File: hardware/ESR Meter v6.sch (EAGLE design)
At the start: 34 parts, among them Q1 MOSFET-NCHANNELFQP30N06L, U1 ATMEGA328P, U2 3V3, U3 LM317, Y1 8M

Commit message: Update library used for L4931
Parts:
- U2: device RBBB:L4931 -> l4931:L4931
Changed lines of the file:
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@@
 <part name="R2" library="resistor" deviceset="R-US_" device="0207/10" value="2.2k"/>
 <part name="SUPPLY1" library="supply2" deviceset="GND" device=""/>
-<part name="U2" library="RBBB" deviceset="L4931" device="" value="3V3"/>
+<part name="U2" library="l4931" deviceset="L4931" device="" value="3V3"/>
 <part name="C1" library="SparkFun-Capacitors" deviceset="CAP_POL" device="PTH2" value="47u"/>
 <part name="C2" library="SparkFun-Capacitors" deviceset="CAP_POL" device="PTH2" value="47u"/>

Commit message: Rewrote README.md
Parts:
- R8: value 1 -> 1 1%
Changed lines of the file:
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@@
 <part name="SUPPLY9" library="supply2" deviceset="GND" device=""/>
 <part name="Q1" library="SparkFun-DiscreteSemi" deviceset="MOSFET-NCHANNEL" device="FQP30N06L"/>
-<part name="R8" library="resistor" deviceset="R-US_" device="0617/5V" value="1"/>
+<part name="R8" library="resistor" deviceset="R-US_" device="0617/5V" value="1 1%"/>
 <part name="SUPPLY10" library="supply2" deviceset="GND" device=""/>
 <part name="D1" library="diode" deviceset="1N581*" device="" technology="9-B"/>

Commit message: Edited README
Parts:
- Q1: value MOSFET-NCHANNELFQP30N06L -> FQP30N06L
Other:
- moved on the sheet: BATT+, BATT-, C1, C2, JP3, PAD1, PAD2, U2
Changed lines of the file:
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@@
 <part name="LOGO1" library="SparkFun-Aesthetics" deviceset="OSHW-LOGO" device="M"/>
 <part name="SUPPLY9" library="supply2" deviceset="GND" device=""/>
-<part name="Q1" library="SparkFun-DiscreteSemi" deviceset="MOSFET-NCHANNEL" device="FQP30N06L"/>
+<part name="Q1" library="SparkFun-DiscreteSemi" deviceset="MOSFET-NCHANNEL" device="FQP30N06L" value="FQP30N06L"/>
 <part name="R8" library="resistor" deviceset="R-US_" device="0617/5V" value="1 1%"/>
 <part name="SUPPLY10" library="supply2" deviceset="GND" device=""/>
@@
 <text x="-2.54" y="2.54" size="1.778" layer="91" rot="R90">2x16 LCD DISPLAY</text>
 <text x="-2.54" y="81.28" size="1.778" layer="91" rot="R90">SERIAL</text>
-<text x="111.76" y="45.72" size="1.778" layer="91">DISPLAY OPTION
+<text x="109.22" y="43.18" size="1.778" layer="91">DISPLAY OPTION
 JUMPER</text>
 </plain>
@@
 <instance part="R1" gate="G$1" x="139.7" y="66.04" rot="R270"/>
 <instance part="R2" gate="G$1" x="124.46" y="55.88"/>
-<instance part="SUPPLY1" gate="GND" x="182.88" y="48.26"/>
-<instance part="U2" gate="1" x="157.48" y="15.24"/>
-<instance part="C1" gate="G$1" x="167.64" y="10.16"/>
-<instance part="C2" gate="G$1" x="147.32" y="10.16"/>
-<instance part="PAD1" gate="1" x="144.78" y="15.24"/>
-<instance part="SUPPLY3" gate="GND" x="157.48" y="-2.54"/>
-<instance part="SUPPLY4" gate="G$1" x="167.64" y="15.24"/>
+<instance part="SUPPLY1" gate="GND" x="180.34" y="60.96"/>
+<instance part="U2" gate="1" x="132.08" y="10.16"/>
+<instance part="C1" gate="G$1" x="142.24" y="5.08"/>
+<instance part="C2" gate="G$1" x="121.92" y="5.08"/>
+<instance part="PAD1" gate="1" x="119.38" y="10.16"/>
+<instance part="SUPPLY3" gate="GND" x="132.08" y="-7.62"/>
+<instance part="SUPPLY4" gate="G$1" x="142.24" y="10.16"/>
 <instance part="C3" gate="G$1" x="114.3" y="104.14"/>
 <instance part="R3" gate="G$1" x="114.3" y="86.36" rot="R90"/>
@@
 <instance part="SUPPLY12" gate="GND" x="10.16" y="-30.48"/>
 <instance part="SUPPLY14" gate="G$1" x="25.4" y="-22.86"/>
-<instance part="PAD2" gate="1" x="144.78" y="2.54"/>
+<instance part="PAD2" gate="1" x="119.38" y="-2.54"/>
 <instance part="S+" gate="1" x="114.3" y="109.22" smashed="yes" rot="R270">
 <attribute name="NAME" x="110.617" y="111.0742" size="1.778" layer="95"/>
 </instance>
-<instance part="BATT+" gate="G$1" x="187.96" y="71.12" smashed="yes" rot="R180">
-<attribute name="NAME" x="189.103" y="69.2658" size="1.778" layer="95" rot="R180"/>
-<attribute name="VALUE" x="206.883" y="74.422" size="1.778" layer="96" rot="R180"/>
-</instance>
-<instance part="BATT-" gate="G$1" x="187.96" y="50.8" rot="R180"/>
+<instance part="BATT+" gate="G$1" x="185.42" y="71.12" smashed="yes" rot="R180">
+<attribute name="NAME" x="196.723" y="71.8058" size="1.778" layer="95" rot="R180"/>
+</instance>
+<instance part="BATT-" gate="G$1" x="185.42" y="63.5" smashed="yes" rot="R180">
+<attribute name="NAME" x="196.723" y="64.1858" size="1.778" layer="95" rot="R180"/>
+</instance>
 <instance part="S-" gate="1" x="127" y="109.22" smashed="yes" rot="R270">
 <attribute name="NAME" x="123.317" y="111.0742" size="1.778" layer="95"/>
@@
 <instance part="R7" gate="G$1" x="127" y="86.36" rot="R90"/>
 <instance part="SUPPLY2" gate="GND" x="127" y="78.74"/>
-<instance part="JP1" gate="A" x="106.68" y="53.34" rot="R270"/>
+<instance part="JP1" gate="A" x="106.68" y="53.34" smashed="yes" rot="R270">
+<attribute name="NAME" x="109.22" y="49.53" size="1.778" layer="95"/>
+<attribute name="VALUE" x="106.68" y="47.625" size="1.778" layer="96"/>
+</instance>
 <instance part="SUPPLY15" gate="GND" x="104.14" y="48.26"/>
 <instance part="LOGO1" gate="G$1" x="20.32" y="43.18"/>
 <instance part="SUPPLY9" gate="GND" x="170.18" y="60.96"/>
-<instance part="Q1" gate="G$1" x="139.7" y="55.88"/>
+<instance part="Q1" gate="G$1" x="139.7" y="55.88" smashed="yes">
+<attribute name="NAME" x="144.78" y="58.42" size="1.778" layer="95"/>
+<attribute name="VALUE" x="144.78" y="55.88" size="1.778" layer="96"/>
+</instance>
 <instance part="R8" gate="G$1" x="139.7" y="43.18" rot="R270"/>
 <instance part="SUPPLY10" gate="GND" x="139.7" y="33.02"/>
@@
 </instance>
 <instance part="C7" gate="G$1" x="170.18" y="66.04"/>
-<instance part="JP3" gate="A" x="147.32" y="25.4"/>
+<instance part="JP3" gate="A" x="121.92" y="20.32"/>
 <instance part="C9" gate="G$1" x="35.56" y="81.28"/>
 <instance part="SUPPLY16" gate="GND" x="35.56" y="76.2"/>
@@
 <pinref part="U2" gate="1" pin="GND"/>
 <pinref part="SUPPLY3" gate="GND" pin="GND"/>
-<wire x1="157.48" y1="7.62" x2="157.48" y2="2.54" width="0.1524" layer="91"/>
+<wire x1="132.08" y1="2.54" x2="132.08" y2="-2.54" width="0.1524" layer="91"/>
 <pinref part="C2" gate="G$1" pin="-"/>
-<wire x1="157.48" y1="2.54" x2="157.48" y2="0" width="0.1524" layer="91"/>
-<wire x1="147.32" y1="5.08" x2="147.32" y2="2.54" width="0.1524" layer="91"/>
-<wire x1="147.32" y1="2.54" x2="157.48" y2="2.54" width="0.1524" layer="91"/>
+<wire x1="132.08" y1="-2.54" x2="132.08" y2="-5.08" width="0.1524" layer="91"/>
+<wire x1="121.92" y1="0" x2="121.92" y2="-2.54" width="0.1524" layer="91"/>
+<wire x1="121.92" y1="-2.54" x2="132.08" y2="-2.54" width="0.1524" layer="91"/>
 <pinref part="C1" gate="G$1" pin="-"/>
-<wire x1="157.48" y1="2.54" x2="167.64" y2="2.54" width="0.1524" layer="91"/>
-<wire x1="167.64" y1="2.54" x2="167.64" y2="5.08" width="0.1524" layer="91"/>
-<junction x="157.48" y="2.54"/>
+<wire x1="132.08" y1="-2.54" x2="142.24" y2="-2.54" width="0.1524" layer="91"/>
+<wire x1="142.24" y1="-2.54" x2="142.24" y2="0" width="0.1524" layer="91"/>
+<junction x="132.08" y="-2.54"/>
 <pinref part="PAD2" gate="1" pin="P"/>
-<junction x="147.32" y="2.54"/>
+<junction x="121.92" y="-2.54"/>
 </segment>
 <segment>
@@
 <segment>
 <pinref part="BATT-" gate="G$1" pin="P"/>
-<wire x1="185.42" y1="50.8" x2="182.88" y2="50.8" width="0.1524" layer="91"/>
+<wire x1="182.88" y1="63.5" x2="180.34" y2="63.5" width="0.1524" layer="91"/>
 <pinref part="SUPPLY1" gate="GND" pin="GND"/>
 </segment>
@@
 <pinref part="U2" gate="1" pin="IN"/>
 <pinref part="PAD1" gate="1" pin="P"/>
-<wire x1="149.86" y1="15.24" x2="147.32" y2="15.24" width="0.1524" layer="91"/>
+<wire x1="124.46" y1="10.16" x2="121.92" y2="10.16" width="0.1524" layer="91"/>
 <pinref part="C2" gate="G$1" pin="+"/>
-<wire x1="147.32" y1="12.7" x2="147.32" y2="15.24" width="0.1524" layer="91"/>
-<junction x="147.32" y="15.24"/>
+<wire x1="121.92" y1="7.62" x2="121.92" y2="10.16" width="0.1524" layer="91"/>
+<junction x="121.92" y="10.16"/>
 <pinref part="JP3" gate="A" pin="1"/>
-<wire x1="147.32" y1="15.24" x2="147.32" y2="22.86" width="0.1524" layer="91"/>
+<wire x1="121.92" y1="10.16" x2="121.92" y2="17.78" width="0.1524" layer="91"/>
 </segment>
 </net>
@@
 <segment>
 <pinref part="U2" gate="1" pin="OUT"/>
-<wire x1="165.1" y1="15.24" x2="167.64" y2="15.24" width="0.1524" layer="91"/>
+<wire x1="139.7" y1="10.16" x2="142.24" y2="10.16" width="0.1524" layer="91"/>
 <pinref part="C1" gate="G$1" pin="+"/>
-<wire x1="167.64" y1="15.24" x2="167.64" y2="12.7" width="0.1524" layer="91"/>
+<wire x1="142.24" y1="10.16" x2="142.24" y2="7.62" width="0.1524" layer="91"/>
 <pinref part="SUPPLY4" gate="G$1" pin="5V"/>
-<junction x="167.64" y="15.24"/>
+<junction x="142.24" y="10.16"/>
 </segment>
 <segment>
@@
 <pinref part="BATT+" gate="G$1" pin="P"/>
 <pinref part="D1" gate="G$1" pin="A"/>
-<wire x1="185.42" y1="71.12" x2="180.34" y2="71.12" width="0.1524" layer="91"/>
+<wire x1="182.88" y1="71.12" x2="180.34" y2="71.12" width="0.1524" layer="91"/>
 </segment>
 <segment>
 <pinref part="JP3" gate="A" pin="2"/>
-<wire x1="149.86" y1="22.86" x2="175.26" y2="22.86" width="0.1524" layer="91"/>
-<label x="175.26" y="22.86" size="1.778" layer="95" xref="yes"/>
-</segment>
-</net>
+<wire x1="124.46" y1="17.78" x2="149.86" y2="17.78" width="0.1524" layer="91"/>
+<label x="149.86" y="17.78" size="1.778" layer="95" xref="yes"/>
+</segment>
+</net>

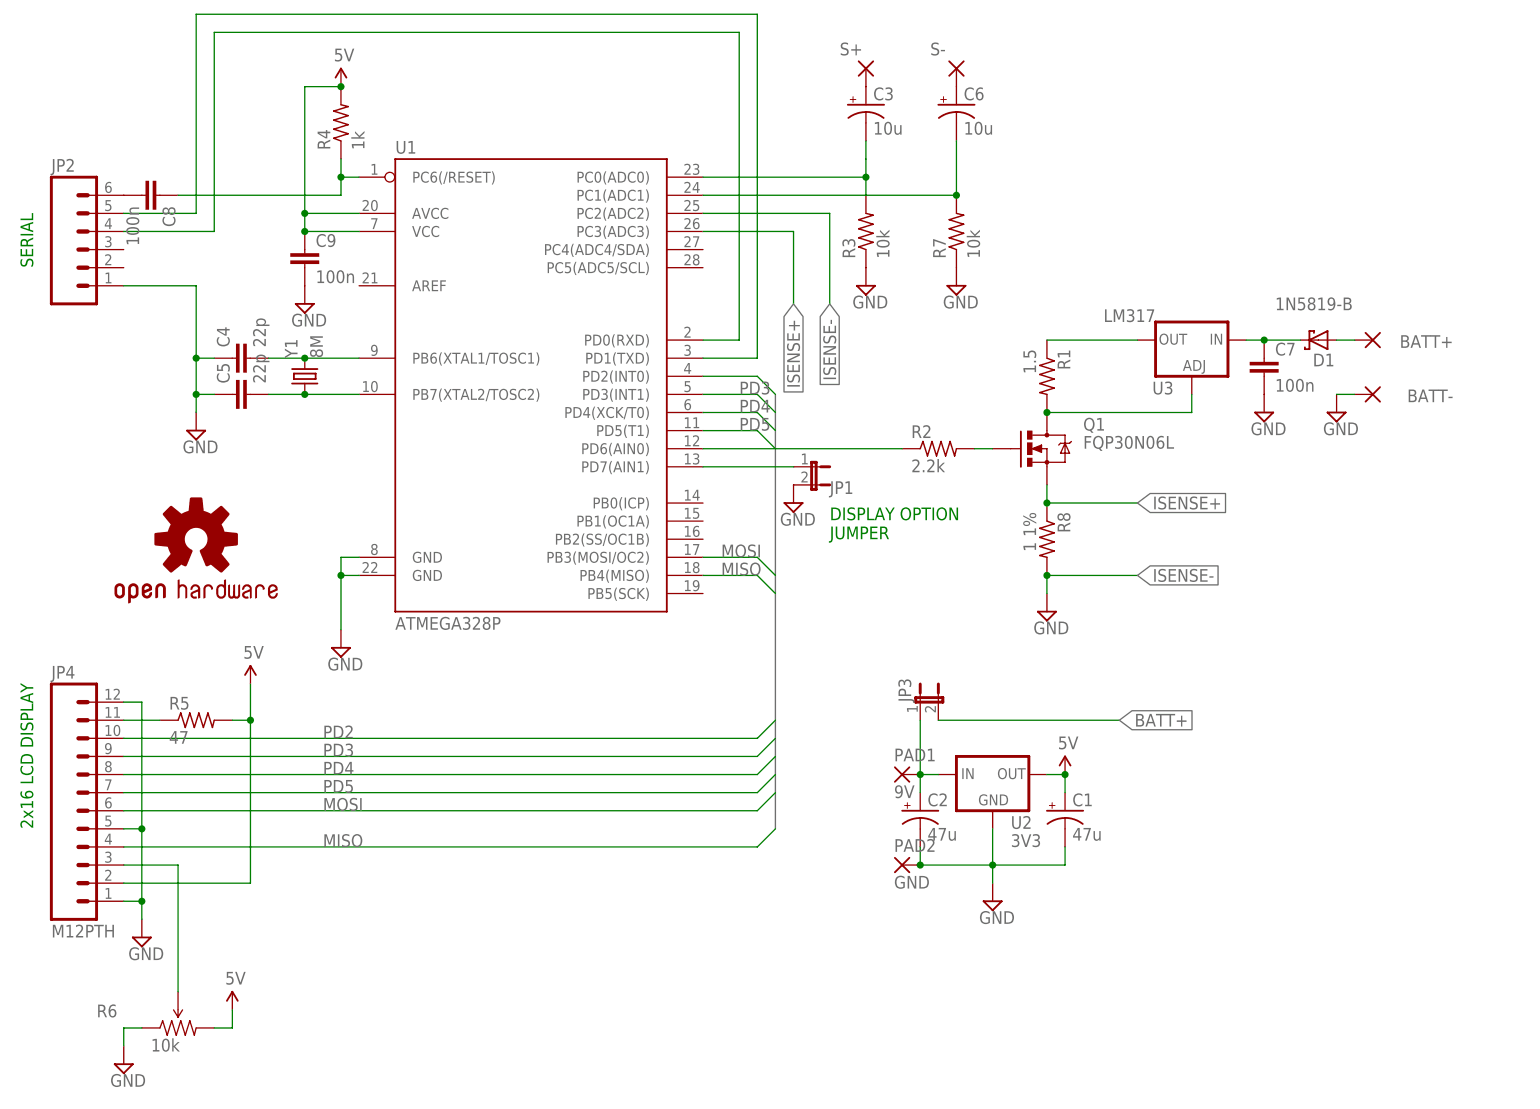
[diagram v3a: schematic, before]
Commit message: Added BOM. Minor changes to schematics and board.
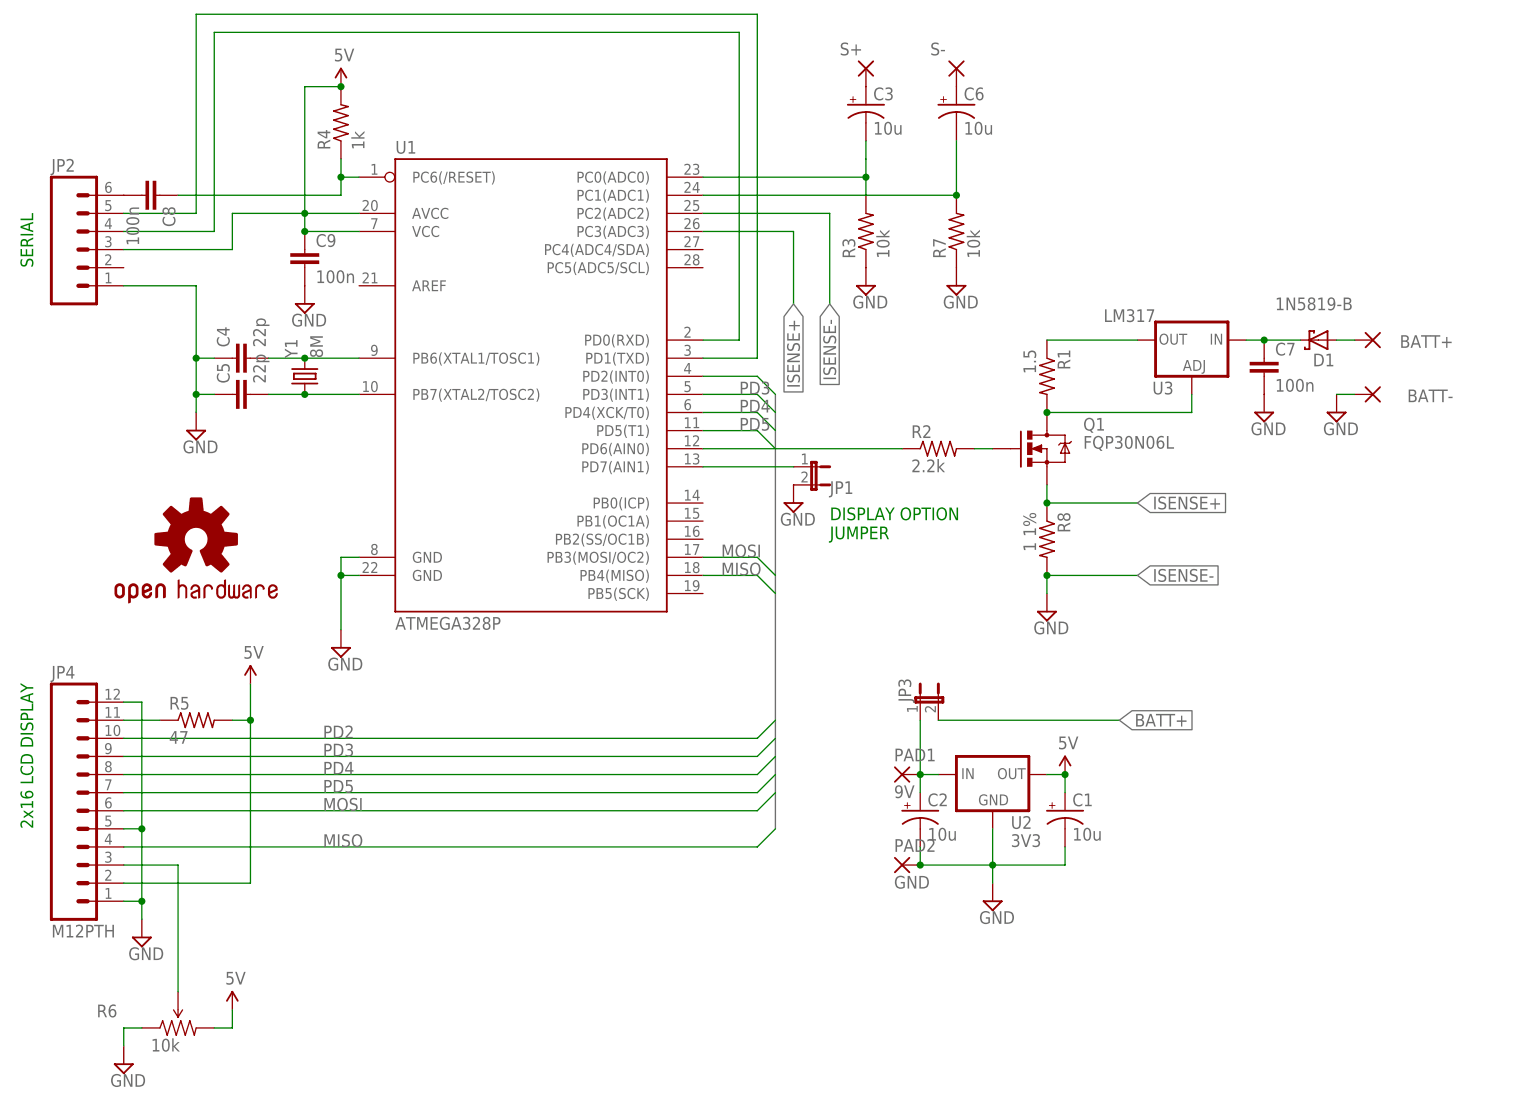
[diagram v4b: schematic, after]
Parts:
- C1, C2: value 47u -> 10u
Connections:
- net 5V: now also JP2.3
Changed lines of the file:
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@@
 <part name="SUPPLY1" library="supply2" deviceset="GND" device=""/>
 <part name="U2" library="l4931" deviceset="L4931" device="" value="3V3"/>
-<part name="C1" library="SparkFun-Capacitors" deviceset="CAP_POL" device="PTH2" value="47u"/>
-<part name="C2" library="SparkFun-Capacitors" deviceset="CAP_POL" device="PTH2" value="47u"/>
+<part name="C1" library="SparkFun-Capacitors" deviceset="CAP_POL" device="PTH2" value="10u"/>
+<part name="C2" library="SparkFun-Capacitors" deviceset="CAP_POL" device="PTH2" value="10u"/>
 <part name="PAD1" library="wirepad" deviceset="1,6/0,9" device="" value="9V"/>
 <part name="SUPPLY3" library="supply2" deviceset="GND" device=""/>
@@
 <pinref part="C9" gate="G$1" pin="1"/>
 <junction x="35.56" y="86.36"/>
-</segment>
-<segment>
+<pinref part="JP2" gate="G$1" pin="3"/>
+<wire x1="10.16" y1="83.82" x2="25.4" y2="83.82" width="0.1524" layer="91"/>
+<wire x1="25.4" y1="83.82" x2="25.4" y2="88.9" width="0.1524" layer="91"/>
+<wire x1="25.4" y1="88.9" x2="35.56" y2="88.9" width="0.1524" layer="91"/>
+</segment>
+<segment>
